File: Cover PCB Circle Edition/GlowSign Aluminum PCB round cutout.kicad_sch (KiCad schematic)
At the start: 4 parts, among them U1 SMTSO3030CTJ, U2 SMTSO3030CTJ, U3 SMTSO3030CTJ, U4 SMTSO3030CTJ

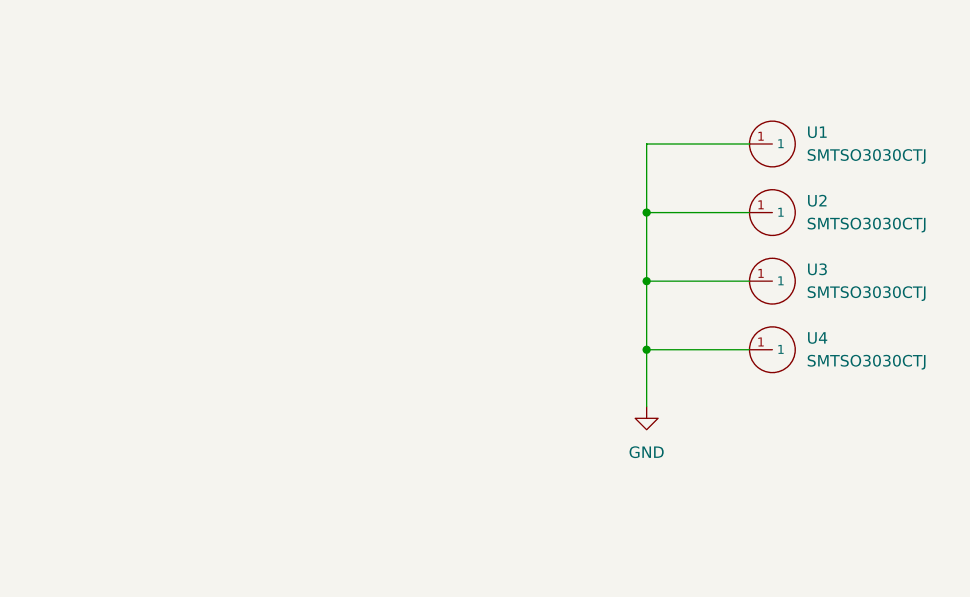
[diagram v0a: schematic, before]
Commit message: updated cover circle pcb
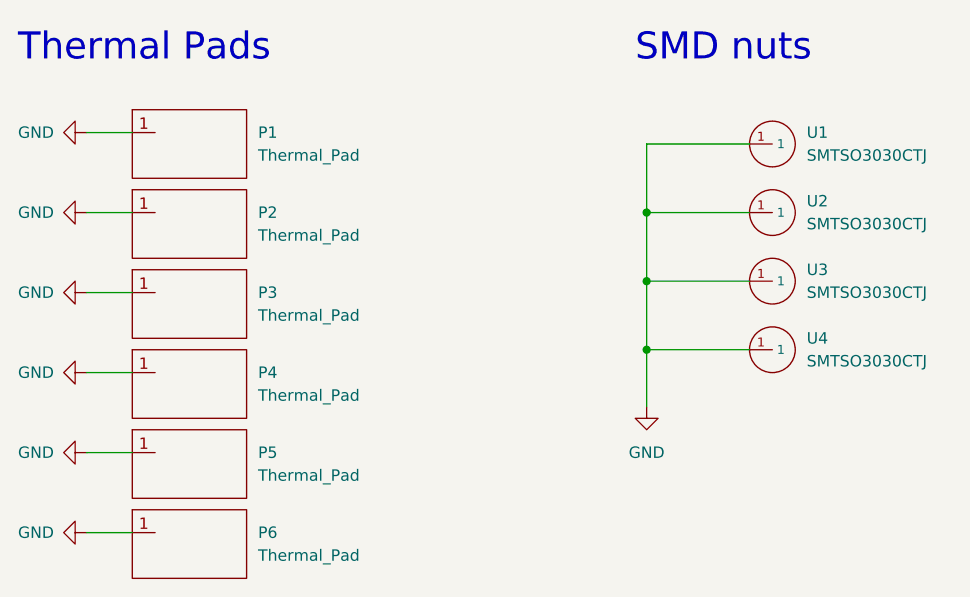
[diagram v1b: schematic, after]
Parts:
- added P1, P2, P3, P4, P5, P6: Thermal_Pad, footprint:Thermal pad, symbol MyParts:Thermal_Pad
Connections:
- net GND: now also P1.1, P2.1, P3.1, P4.1, P5.1, P6.1
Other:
- note added: "SMD nuts"
- note added: "Thermal Pads"

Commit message: separated battery electronics into separate pcb
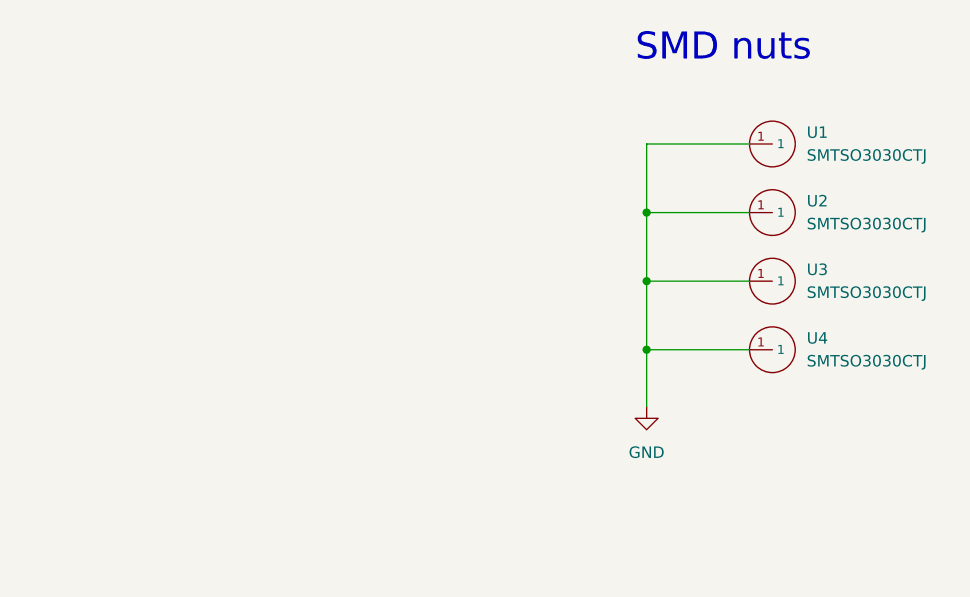
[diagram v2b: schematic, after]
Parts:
- removed P1, P2, P3, P4, P5, P6: Thermal_Pad, footprint:Thermal pad, symbol MyParts:Thermal_Pad
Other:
- note removed: "Thermal Pads"
